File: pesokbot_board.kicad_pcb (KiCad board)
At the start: 2 copper layers, 32 parts, among them J1 J_BAT_3S2P, Q1 SQJQ100E, U1 LM74700

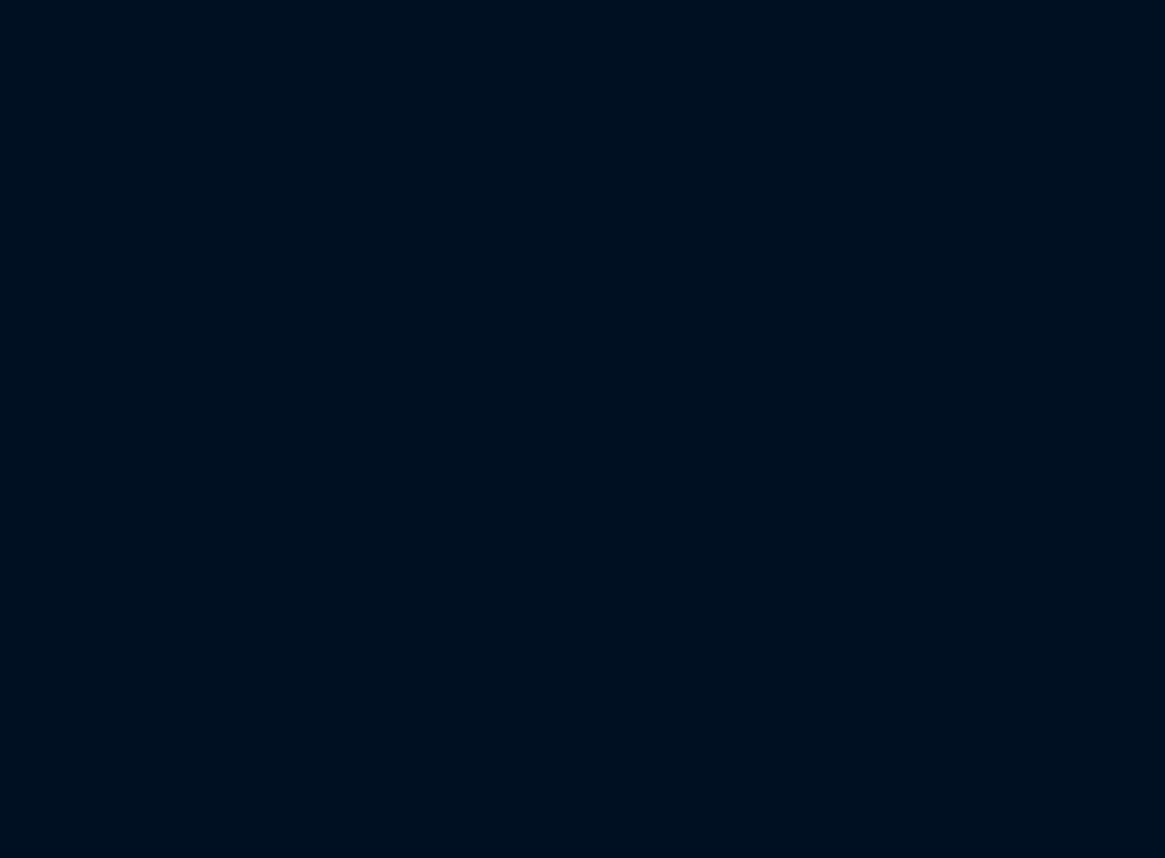
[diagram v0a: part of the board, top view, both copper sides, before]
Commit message: added footprints and connect usb33c MCU to power and VREF+ to REF3033
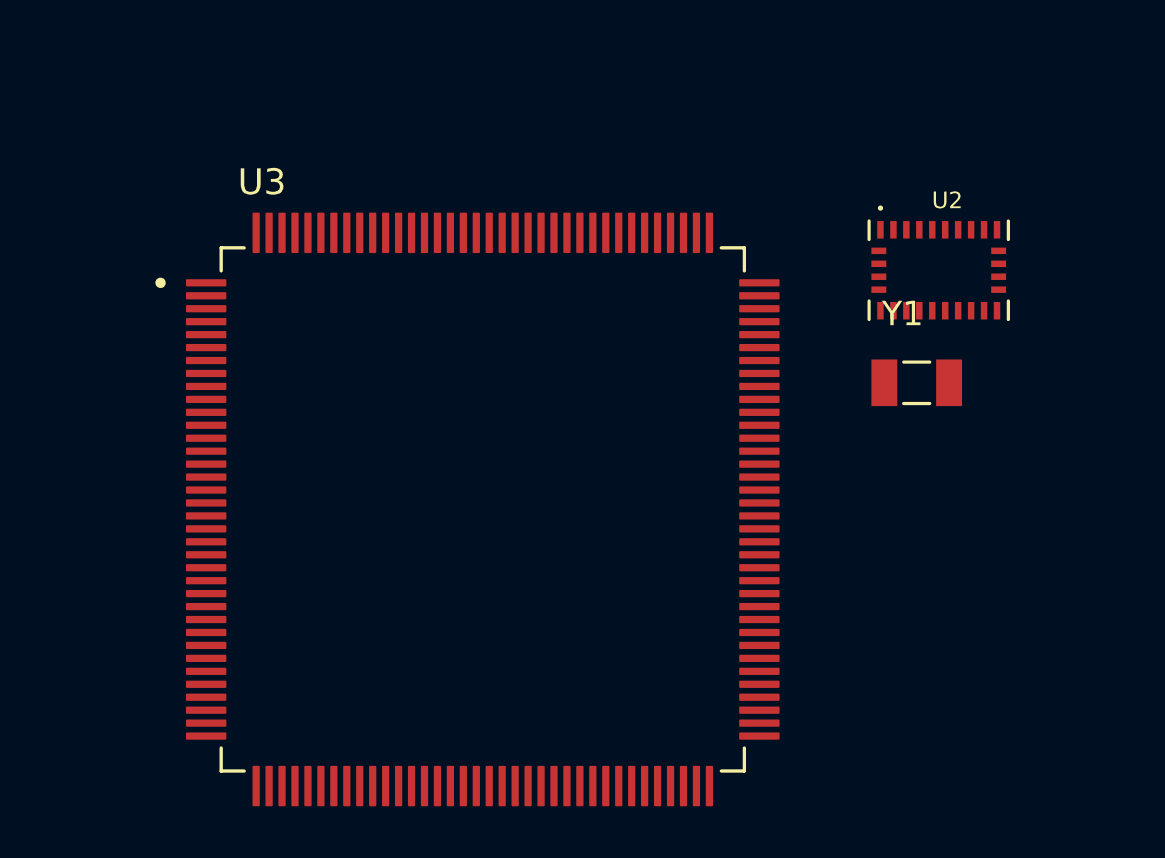
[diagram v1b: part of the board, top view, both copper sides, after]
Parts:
- added U2: BNO086, BNO086:IC_BNO086, F.Cu at (-32.0, 110.2)
- added U3: STM32H743ZIT6, STM32H743ZIT6:QFP50P2200X2200X160, F.Cu at (-49.6, 119.5)
- added Y1: FC-135_32.7680KA-A0, FC135:XTAL_FC-135_32.7680KA-A0, F.Cu at (-32.9, 114.6)

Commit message: added usb mcu and footprints
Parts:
- added C20: 100nF, Capacitor_SMD:C_0805_2012Metric_Pad1.18x1.45mm_HandSolder, F.Cu at (-92.8, 74.0)
- added C21: 4.7 µF, Capacitor_SMD:C_0805_2012Metric_Pad1.18x1.45mm_HandSolder, F.Cu at (-92.8, 77.0)
- added C22: 100nF, Capacitor_SMD:C_0805_2012Metric_Pad1.18x1.45mm_HandSolder, F.Cu at (-92.8, 80.0)
- added P1: USB_C_Plug_USB2.0, Connector_USB:USB_C_Receptacle_HRO_TYPE-C-31-M-12, F.Cu at (82.7, 85.8)
- added P2: USB_C_Plug_USB2.0, Connector_USB:USB_C_Receptacle_HRO_TYPE-C-31-M-12, F.Cu at (-81.9, 111.3)
- added U4: REF3033, Package_TO_SOT_SMD:SOT-23, F.Cu at (-81.2, 67.0)
- moved U3 9.19 mm to (-53.7, 111.2)
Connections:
- U3 pad 103: unconnected-(U3A-PA11-Pad103) -> DM_USBC
- U3 pad 104: unconnected-(U3A-PA12-Pad104) -> DP_USBC
- U3 pad 32: unconnected-(U3A-VREF+-Pad32) -> ref3033
- U3 pad 95: unconnected-(U3A-VDD33USB-Pad95) -> +3V3
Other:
- board outline added: 126 x 53.2 mm

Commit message: added edge cuts
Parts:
- moved U3 201.7 mm to (147.6, 98.2)
- moved U2 199.3 mm to (167.0, 98.7), turned to -90 degrees
- moved P1 30.8 mm to (52.0, 88.0)
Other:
- board size 126 x 53.2 mm -> 70 x 50 mm
- copper layers 2 -> 4

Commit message: start place components
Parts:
- added R1: R, Resistor_SMD:R_0805_2012Metric_Pad1.20x1.40mm_HandSolder, F.Cu at (123.0, 117.0)
- moved P2 260.7 mm to (178.8, 108.2), turned to 90 degrees
- moved R10 226.7 mm to (156.0, 104.2), turned to -90 degrees
- moved R7 226.0 mm to (153.2, 104.2), turned to 90 degrees
- moved R6 223.9 mm to (150.2, 104.2), turned to 90 degrees
- moved R11 218.3 mm to (149.2, 98.0), turned to 180 degrees
- moved C11 213.5 mm to (162.5, 98.8)
- moved C12 212.4 mm to (162.5, 96.0), turned to 180 degrees
- moved C10 206.9 mm to (156.5, 92.5)
- moved C9 206.9 mm to (156.5, 89.5)
- moved C19 201.8 mm to (141.2, 117.5), turned to 90 degrees
- moved C16 201.4 mm to (138.0, 117.5), turned to 90 degrees
- moved C15 199.5 mm to (135.0, 117.5), turned to 90 degrees
- moved C13 198.8 mm to (132.0, 117.5), turned to 90 degrees
- moved Y1 192.1 mm to (158.5, 97.2), turned to -90 degrees
- moved C18 182.5 mm to (120.3, 117.0), turned to 90 degrees
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
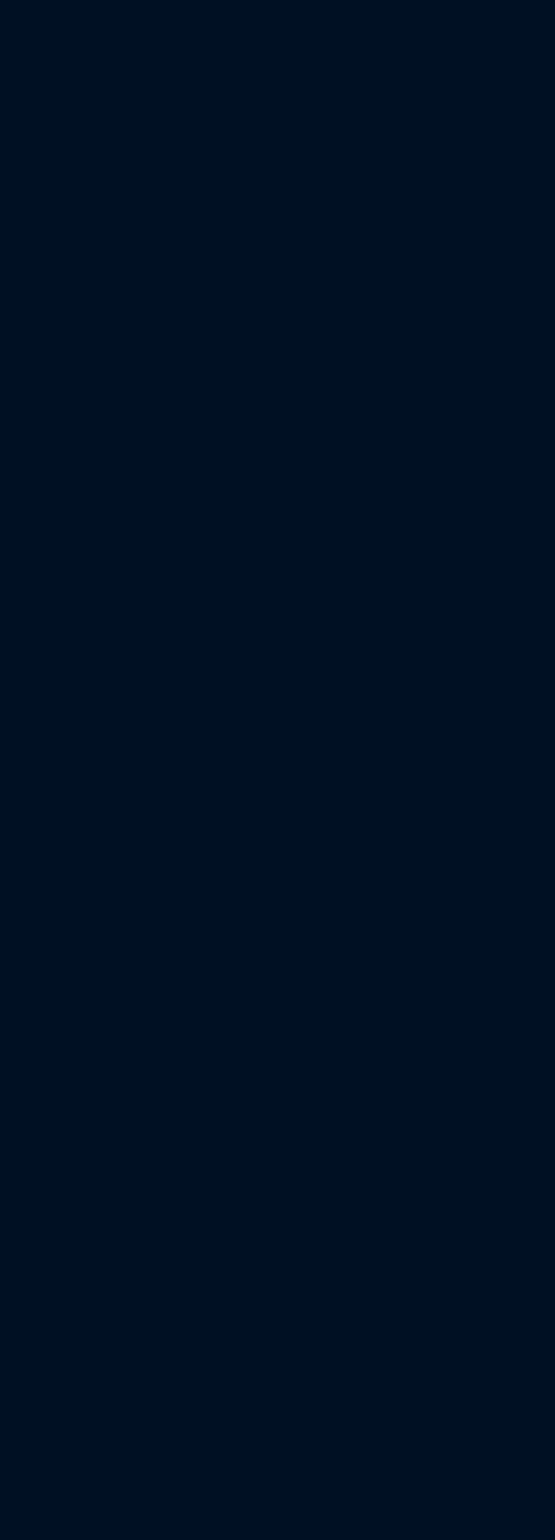
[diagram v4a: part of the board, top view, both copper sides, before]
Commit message: added user ports
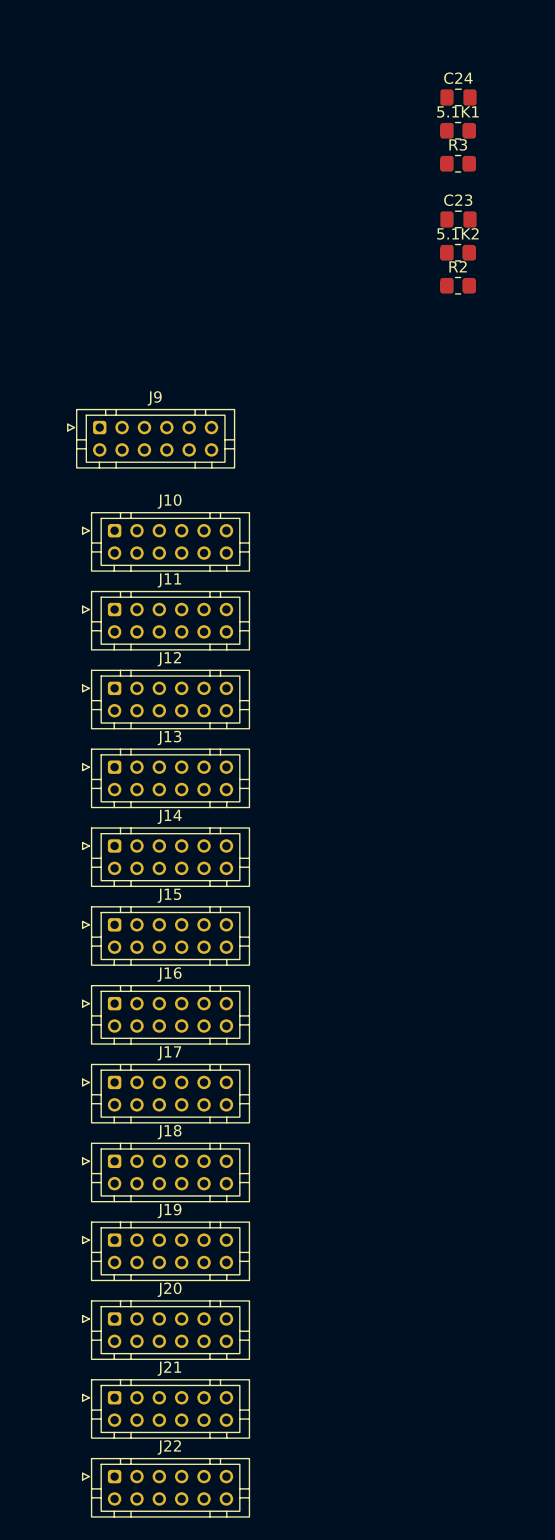
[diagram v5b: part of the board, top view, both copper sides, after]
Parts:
- added 5.1K1: R, Resistor_SMD:R_0805_2012Metric_Pad1.20x1.40mm_HandSolder, F.Cu at (-39.5, 88.2)
- added 5.1K2: R, Resistor_SMD:R_0805_2012Metric_Pad1.20x1.40mm_HandSolder, F.Cu at (-39.5, 99.1)
- added C23: 10nF, Capacitor_SMD:C_0805_2012Metric_Pad1.18x1.45mm_HandSolder, F.Cu at (-39.5, 96.2)
- added C24: 10nF, Capacitor_SMD:C_0805_2012Metric_Pad1.18x1.45mm_HandSolder, F.Cu at (-39.5, 85.2)
- added J10: Conn_02x06_Odd_Even, Connector_JST:JST_PHD_B12B-PHDSS_2x06_P2.00mm_Vertical, F.Cu at (-70.2, 124.0)
- added J11: Conn_02x06_Odd_Even, Connector_JST:JST_PHD_B12B-PHDSS_2x06_P2.00mm_Vertical, F.Cu at (-70.2, 131.1)
- added J12: Conn_02x06_Odd_Even, Connector_JST:JST_PHD_B12B-PHDSS_2x06_P2.00mm_Vertical, F.Cu at (-70.2, 138.1)
- added J13: Conn_02x06_Odd_Even, Connector_JST:JST_PHD_B12B-PHDSS_2x06_P2.00mm_Vertical, F.Cu at (-70.2, 145.2)
- added J14: Conn_02x06_Odd_Even, Connector_JST:JST_PHD_B12B-PHDSS_2x06_P2.00mm_Vertical, F.Cu at (-70.2, 152.2)
- added J15: Conn_02x06_Odd_Even, Connector_JST:JST_PHD_B12B-PHDSS_2x06_P2.00mm_Vertical, F.Cu at (-70.2, 159.2)
- added J16: Conn_02x06_Odd_Even, Connector_JST:JST_PHD_B12B-PHDSS_2x06_P2.00mm_Vertical, F.Cu at (-70.2, 166.3)
- added J17: Conn_02x06_Odd_Even, Connector_JST:JST_PHD_B12B-PHDSS_2x06_P2.00mm_Vertical, F.Cu at (-70.2, 173.3)
- added J18: Conn_02x06_Odd_Even, Connector_JST:JST_PHD_B12B-PHDSS_2x06_P2.00mm_Vertical, F.Cu at (-70.2, 180.4)
- added J19: Conn_02x06_Odd_Even, Connector_JST:JST_PHD_B12B-PHDSS_2x06_P2.00mm_Vertical, F.Cu at (-70.2, 187.4)
- added J20: Conn_02x06_Odd_Even, Connector_JST:JST_PHD_B12B-PHDSS_2x06_P2.00mm_Vertical, F.Cu at (-70.2, 194.5)
- added J21: Conn_02x06_Odd_Even, Connector_JST:JST_PHD_B12B-PHDSS_2x06_P2.00mm_Vertical, F.Cu at (-70.2, 201.6)
- added J22: Conn_02x06_Odd_Even, Connector_JST:JST_PHD_B12B-PHDSS_2x06_P2.00mm_Vertical, F.Cu at (-70.2, 208.6)
- added J9: Conn_02x06_Odd_Even, Connector_JST:JST_PHD_B12B-PHDSS_2x06_P2.00mm_Vertical, F.Cu at (-71.6, 114.8)
- added R2: 1M, Resistor_SMD:R_0805_2012Metric_Pad1.20x1.40mm_HandSolder, F.Cu at (-39.5, 102.1)
- added R3: 1M, Resistor_SMD:R_0805_2012Metric_Pad1.20x1.40mm_HandSolder, F.Cu at (-39.5, 91.2)

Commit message: added mount vias and start placement uports
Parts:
- removed J22: Conn_02x06_Odd_Even, Connector_JST:JST_PHD_B12B-PHDSS_2x06_P2.00mm_Vertical
- added REF**: MountingHole_3.2mm_M3, MountingHole:MountingHole_3.2mm_M3, F.Cu at (175.0, 125.0)
- added REF**: MountingHole_3.2mm_M3, MountingHole:MountingHole_3.2mm_M3, F.Cu at (105.0, 125.0)
- added REF**: MountingHole_3.2mm_M3, MountingHole:MountingHole_3.2mm_M3, F.Cu at (105.0, 75.0)
- added REF**: MountingHole_3.2mm_M3, MountingHole:MountingHole_3.2mm_M3, F.Cu at (175.0, 75.0)
- moved J10 207.1 mm to (131.0, 75.0)
- moved J9 190.7 mm to (115.2, 76.5)
- moved C13 4.35 mm to (132.1, 113.2)
- moved C15 4.35 mm to (135.1, 113.2)
- moved C16 4.35 mm to (138.1, 113.2)
- moved C17 4.35 mm to (117.4, 112.7)
- moved C18 4.35 mm to (120.4, 112.7)
- moved C19 4.35 mm to (141.4, 113.2)
- moved R1 4.35 mm to (123.1, 112.7)
- moved C14 3.53 mm to (116.5, 83.8)
- moved P1 1.27 mm to (177.5, 87.1)
- moved P2 1.17 mm to (177.6, 108.3)
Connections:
- U3 pad 1: unconnected-(U3C-PE2-Pad1) -> U08_IO2
- U3 pad 10: unconnected-(U3D-PF0-Pad10) -> U10_IO1
- U3 pad 100: unconnected-(U3A-PA8-Pad100) -> U01_IO5
- U3 pad 101: unconnected-(U3A-PA9-Pad101) -> U01_IO6
- U3 pad 102: unconnected-(U3A-PA10-Pad102) -> U01_IO7
- U3 pad 11: unconnected-(U3D-PF1-Pad11) -> U10_IO2
- U3 pad 110: unconnected-(U3A-PA15(JTDI)-Pad110) -> U01_IO8
- U3 pad 111: unconnected-(U3B-PC10-Pad111) -> U05_IO3
- U3 pad 112: unconnected-(U3B-PC11-Pad112) -> U05_IO4
- U3 pad 113: unconnected-(U3B-PC12-Pad113) -> U05_IO5
- U3 pad 114: unconnected-(U3C-PD0-Pad114) -> U03_IO5
- U3 pad 115: unconnected-(U3C-PD1-Pad115) -> U03_IO6
- U3 pad 116: unconnected-(U3C-PD2-Pad116) -> U03_IO7
- U3 pad 117: unconnected-(U3C-PD3-Pad117) -> U03_IO8
- U3 pad 118: unconnected-(U3C-PD4-Pad118) -> U06_IO1
- U3 pad 119: unconnected-(U3C-PD5-Pad119) -> U06_IO2
- U3 pad 12: unconnected-(U3D-PF2-Pad12) -> U10_IO3
- U3 pad 122: unconnected-(U3C-PD6-Pad122) -> U06_IO3
- U3 pad 123: unconnected-(U3C-PD7-Pad123) -> U06_IO4
- U3 pad 124: unconnected-(U3D-PG9-Pad124) -> U13_IO2
- U3 pad 125: unconnected-(U3D-PG10-Pad125) -> U13_IO3
- U3 pad 126: unconnected-(U3D-PG11-Pad126) -> U13_IO4
- U3 pad 127: unconnected-(U3D-PG12-Pad127) -> U13_IO5
- U3 pad 128: unconnected-(U3D-PG13-Pad128) -> U13_IO6
- U3 pad 129: unconnected-(U3D-PG14-Pad129) -> U13_IO7
- U3 pad 13: unconnected-(U3D-PF3-Pad13) -> U10_IO4
- U3 pad 132: unconnected-(U3D-PG15-Pad132) -> U13_IO8
- U3 pad 133: unconnected-(U3B-PB3(JTDO/TRACESWO)-Pad133) -> U02_IO1
- U3 pad 134: unconnected-(U3B-PB4(~{JTRST})-Pad134) -> U02_IO2
- U3 pad 135: unconnected-(U3B-PB5-Pad135) -> U02_IO3
- U3 pad 136: unconnected-(U3B-PB6-Pad136) -> U02_IO4
- U3 pad 137: unconnected-(U3B-PB7-Pad137) -> U02_IO5
- U3 pad 139: unconnected-(U3B-PB8-Pad139) -> U02_IO6
- U3 pad 14: unconnected-(U3D-PF4-Pad14) -> U10_IO5
- U3 pad 140: unconnected-(U3B-PB9-Pad140) -> U02_IO7
- U3 pad 141: unconnected-(U3C-PE0-Pad141) -> U08_IO1
- U3 pad 142: unconnected-(U3C-PE1-Pad142) -> U08_IO3
- U3 pad 15: unconnected-(U3D-PF5-Pad15) -> U10_IO6
- U3 pad 18: unconnected-(U3D-PF6-Pad18) -> U11_IO1
- U3 pad 19: unconnected-(U3D-PF7-Pad19) -> U11_IO2
- U3 pad 2: unconnected-(U3C-PE3-Pad2) -> U08_IO4
- U3 pad 20: unconnected-(U3D-PF8-Pad20) -> U11_IO3
- U3 pad 21: unconnected-(U3D-PF9-Pad21) -> U11_IO4
- U3 pad 22: unconnected-(U3D-PF10-Pad22) -> U11_IO5
- U3 pad 23: unconnected-(U3A-PH0/OSC_IN-Pad23) -> U07_IO5
- U3 pad 24: unconnected-(U3A-PH1/OSC_OUT-Pad24) -> U07_IO6
- U3 pad 26: unconnected-(U3B-PC0-Pad26) -> U04_IO1
- U3 pad 27: unconnected-(U3B-PC1-Pad27) -> U04_IO2
- U3 pad 28: unconnected-(U3B-PC2_C-Pad28) -> U04_IO3
- U3 pad 29: unconnected-(U3B-PC3_C-Pad29) -> U04_IO4
- U3 pad 3: unconnected-(U3C-PE4-Pad3) -> U08_IO5
- U3 pad 34: unconnected-(U3A-PA0-Pad34) -> U01_IO1
- U3 pad 35: unconnected-(U3A-PA1-Pad35) -> U01_IO2
- U3 pad 36: unconnected-(U3A-PA2-Pad36) -> U01_IO3
- U3 pad 37: unconnected-(U3A-PA3-Pad37) -> U01_IO4
- U3 pad 4: unconnected-(U3C-PE5-Pad4) -> U08_IO6
- U3 pad 44: unconnected-(U3B-PC4-Pad44) -> U04_IO5
- U3 pad 45: unconnected-(U3B-PC5-Pad45) -> U04_IO6
- U3 pad 49: unconnected-(U3D-PF11-Pad49) -> U11_IO6
- U3 pad 5: unconnected-(U3C-PE6-Pad5) -> U08_IO7
- U3 pad 50: unconnected-(U3D-PF12-Pad50) -> U11_IO7
- U3 pad 53: unconnected-(U3D-PF13-Pad53) -> U11_IO8
- U3 pad 54: unconnected-(U3D-PF14-Pad54) -> U10_IO7
- U3 pad 55: unconnected-(U3D-PF15-Pad55) -> U10_IO8
- U3 pad 56: unconnected-(U3D-PG0-Pad56) -> U12_IO1
- U3 pad 57: unconnected-(U3D-PG1-Pad57) -> U12_IO2
- U3 pad 58: unconnected-(U3C-PE7-Pad58) -> U08_IO8
- U3 pad 59: unconnected-(U3C-PE8-Pad59) -> U09_IO1
- U3 pad 60: unconnected-(U3C-PE9-Pad60) -> U09_IO2
- U3 pad 63: unconnected-(U3C-PE10-Pad63) -> U09_IO3
- U3 pad 64: unconnected-(U3C-PE11-Pad64) -> U09_IO4
- U3 pad 65: unconnected-(U3C-PE12-Pad65) -> U09_IO5
- U3 pad 66: unconnected-(U3C-PE13-Pad66) -> U09_IO6
- U3 pad 67: unconnected-(U3C-PE14-Pad67) -> U09_IO7
- U3 pad 68: unconnected-(U3C-PE15-Pad68) -> U09_IO8
- U3 pad 7: unconnected-(U3B-PC13-Pad7) -> U05_IO6
- U3 pad 70: unconnected-(U3B-PB11-Pad70) -> U02_IO8
- U3 pad 73: unconnected-(U3B-PB12-Pad73) -> U03_IO1
- U3 pad 74: unconnected-(U3B-PB13-Pad74) -> U03_IO2
- U3 pad 75: unconnected-(U3B-PB14-Pad75) -> U03_IO3
- U3 pad 76: unconnected-(U3B-PB15-Pad76) -> U03_IO4
- U3 pad 77: unconnected-(U3C-PD8-Pad77) -> U06_IO5
- U3 pad 78: unconnected-(U3C-PD9-Pad78) -> U06_IO6
- U3 pad 79: unconnected-(U3C-PD10-Pad79) -> U06_IO7
- U3 pad 8: unconnected-(U3B-PC14/OSC32_IN-Pad8) -> U05_IO7
- U3 pad 80: unconnected-(U3C-PD11-Pad80) -> U06_IO8
- U3 pad 81: unconnected-(U3C-PD12-Pad81) -> U07_IO1
- U3 pad 82: unconnected-(U3C-PD13-Pad82) -> U07_IO2
- U3 pad 85: unconnected-(U3C-PD14-Pad85) -> U07_IO3
- U3 pad 86: unconnected-(U3C-PD15-Pad86) -> U07_IO4
- U3 pad 87: unconnected-(U3D-PG2-Pad87) -> U12_IO3
- U3 pad 88: unconnected-(U3D-PG3-Pad88) -> U12_IO4
- U3 pad 89: unconnected-(U3D-PG4-Pad89) -> U12_IO5
- U3 pad 9: unconnected-(U3B-PC15/OSC32_OUT-Pad9) -> U05_IO8
- U3 pad 90: unconnected-(U3D-PG5-Pad90) -> U12_IO6
- U3 pad 91: unconnected-(U3D-PG6-Pad91) -> U12_IO7
- U3 pad 92: unconnected-(U3D-PG7-Pad92) -> U12_IO8
- U3 pad 93: unconnected-(U3D-PG8-Pad93) -> U13_IO1
- U3 pad 96: unconnected-(U3B-PC6-Pad96) -> U04_IO7
- U3 pad 97: unconnected-(U3B-PC7-Pad97) -> U04_IO8
- U3 pad 98: unconnected-(U3B-PC8-Pad98) -> U05_IO1
- U3 pad 99: unconnected-(U3B-PC9-Pad99) -> U05_IO2
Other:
- board size 70 x 50 mm -> 80 x 60 mm

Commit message: fix .gitignore
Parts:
- moved J10 1.50 mm to (131.0, 76.5)
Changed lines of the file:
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@@
 		(capping no)
 		(filling no)
-		(zone_defaults)
 		(pcbplotparams
 			(layerselection 0x00000000_00000000_55555555_5755f5ff)
@@
 	(footprint "Connector_JST:JST_PHD_B12B-PHDSS_2x06_P2.00mm_Vertical"
 		(layer "F.Cu")
-		(at 130.99 75)
+		(at 130.99 76.5)
 		(descr "JST PHD series connector, B12B-PHDSS (http://www.jst-mfg.com/product/pdf/eng/ePHD.pdf)")
 		(tags "connector JST PHD vertical")
